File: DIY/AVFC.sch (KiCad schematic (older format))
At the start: 11 parts, among them J1 Conn_01x07, J2 Conn_01x07, J3 DB15_Female, J4 DB25_Male, U1 74AHCT125N, U2 74AHCT125N, U3 74AHCT125N, U4 74AHCT125N

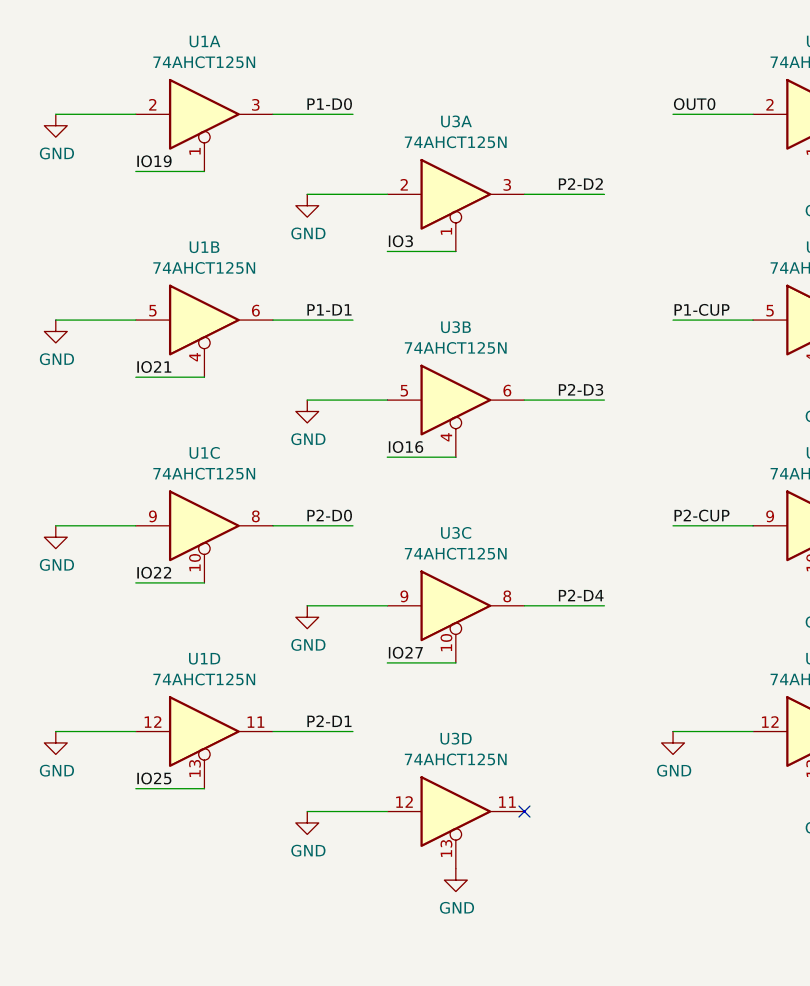
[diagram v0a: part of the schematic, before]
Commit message: Add pullup to OD outputs on ESP side
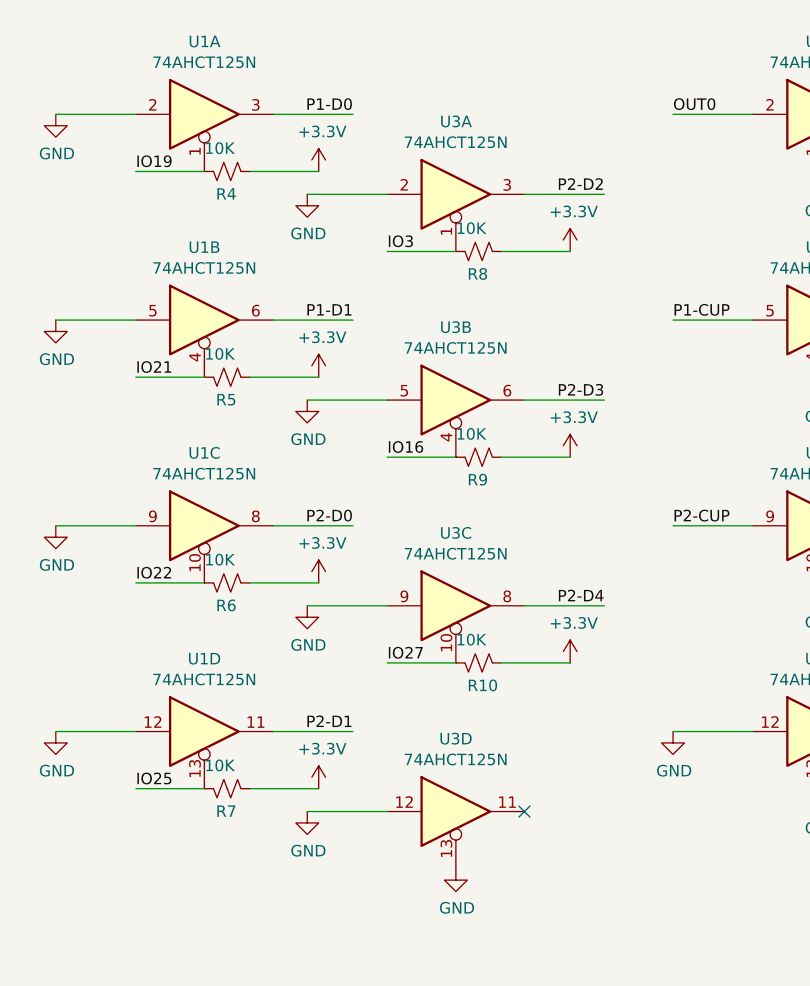
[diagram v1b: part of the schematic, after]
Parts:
- added R10, R4, R5, R6, R7, R8, R9: 10K, symbol Device:R_Small_US
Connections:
- net +3V3: now also R10.1, R4.1, R5.1, R6.1, R7.1, R8.1, R9.1
- net IO16: now also R9.2
- net IO19: now also R4.2
- net IO21: now also R5.2
- net IO22: now also R6.2
- net IO25: now also R7.2
- net IO27: now also R10.2
- net IO3: now also R8.2
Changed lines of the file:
@@
 Text Label 2200 4550 2    50   ~ 0
 P2-D2
+$Comp
+L power:+3.3V #PWR?
+U 1 1 6628EEDA
+P 3950 1600
+AR Path="/5F127084/6628EEDA" Ref="#PWR?"  Part="1"
+AR Path="/5F1E85DD/6628EEDA" Ref="#PWR?"  Part="1"
+AR Path="/65620D27/6628EEDA" Ref="#PWR?"  Part="1"
+F 0 "#PWR?" H 3950 1450 50  0001 C CNN
+F 1 "+3.3V" H 3965 1773 50  0000 C CNN
+F 2 "" H 3950 1600 50  0001 C CNN
+F 3 "" H 3950 1600 50  0001 C CNN
+	1    3950 1600
+	1    0    0    -1
+$EndComp
+$Comp
+L Device:R_Small_US R?
+U 1 1 6628EEE0
+P 3550 1600
+AR Path="/5F1E85DD/6628EEE0" Ref="R?"  Part="1"
+AR Path="/65620D27/6628EEE0" Ref="R4"  Part="1"
+F 0 "R4" V 3450 1550 50  0000 L CNN
+F 1 "10K" V 3650 1500 50  0000 L CNN
+F 2 "" H 3550 1600 50  0001 C CNN
+F 3 "~" H 3550 1600 50  0001 C CNN
+	1    3550 1600
+	0    1    -1   0
+$EndComp
+Wire Wire Line
+	3650 1600 3950 1600
+$Comp
+L power:+3.3V #PWR?
+U 1 1 662932E6
+P 3950 2500
+AR Path="/5F127084/662932E6" Ref="#PWR?"  Part="1"
+AR Path="/5F1E85DD/662932E6" Ref="#PWR?"  Part="1"
+AR Path="/65620D27/662932E6" Ref="#PWR?"  Part="1"
+F 0 "#PWR?" H 3950 2350 50  0001 C CNN
+F 1 "+3.3V" H 3965 2673 50  0000 C CNN
+F 2 "" H 3950 2500 50  0001 C CNN
+F 3 "" H 3950 2500 50  0001 C CNN
+	1    3950 2500
+	1    0    0    -1
+$EndComp
+$Comp
+L Device:R_Small_US R?
+U 1 1 662932EC
+P 3550 2500
+AR Path="/5F1E85DD/662932EC" Ref="R?"  Part="1"
+AR Path="/65620D27/662932EC" Ref="R5"  Part="1"
+F 0 "R5" V 3450 2450 50  0000 L CNN
+F 1 "10K" V 3650 2400 50  0000 L CNN
+F 2 "" H 3550 2500 50  0001 C CNN
+F 3 "~" H 3550 2500 50  0001 C CNN
+	1    3550 2500
+	0    1    -1   0
+$EndComp
+Wire Wire Line
+	3650 2500 3950 2500
+$Comp
+L power:+3.3V #PWR?
+U 1 1 66297501
+P 3950 3400
+AR Path="/5F127084/66297501" Ref="#PWR?"  Part="1"
+AR Path="/5F1E85DD/66297501" Ref="#PWR?"  Part="1"
+AR Path="/65620D27/66297501" Ref="#PWR?"  Part="1"
+F 0 "#PWR?" H 3950 3250 50  0001 C CNN
+F 1 "+3.3V" H 3965 3573 50  0000 C CNN
+F 2 "" H 3950 3400 50  0001 C CNN
+F 3 "" H 3950 3400 50  0001 C CNN
+	1    3950 3400
+	1    0    0    -1
+$EndComp
+$Comp
+L Device:R_Small_US R?
+U 1 1 66297507
+P 3550 3400
+AR Path="/5F1E85DD/66297507" Ref="R?"  Part="1"
+AR Path="/65620D27/66297507" Ref="R6"  Part="1"
+F 0 "R6" V 3450 3350 50  0000 L CNN
+F 1 "10K" V 3650 3300 50  0000 L CNN
+F 2 "" H 3550 3400 50  0001 C CNN
+F 3 "~" H 3550 3400 50  0001 C CNN
+	1    3550 3400
+	0    1    -1   0
+$EndComp
+Wire Wire Line
+	3650 3400 3950 3400
+$Comp
+L power:+3.3V #PWR?
+U 1 1 6629B5CB
+P 3950 4300
+AR Path="/5F127084/6629B5CB" Ref="#PWR?"  Part="1"
+AR Path="/5F1E85DD/6629B5CB" Ref="#PWR?"  Part="1"
+AR Path="/65620D27/6629B5CB" Ref="#PWR?"  Part="1"
+F 0 "#PWR?" H 3950 4150 50  0001 C CNN
+F 1 "+3.3V" H 3965 4473 50  0000 C CNN
+F 2 "" H 3950 4300 50  0001 C CNN
+F 3 "" H 3950 4300 50  0001 C CNN
+	1    3950 4300
+	1    0    0    -1
+$EndComp
+$Comp
+L Device:R_Small_US R?
+U 1 1 6629B5D1
+P 3550 4300
+AR Path="/5F1E85DD/6629B5D1" Ref="R?"  Part="1"
+AR Path="/65620D27/6629B5D1" Ref="R7"  Part="1"
+F 0 "R7" V 3450 4250 50  0000 L CNN
+F 1 "10K" V 3650 4200 50  0000 L CNN
+F 2 "" H 3550 4300 50  0001 C CNN
+F 3 "~" H 3550 4300 50  0001 C CNN
+	1    3550 4300
+	0    1    -1   0
+$EndComp
+Wire Wire Line
+	3650 4300 3950 4300
+$Comp
+L power:+3.3V #PWR?
+U 1 1 6629F3E8
+P 5050 1950
+AR Path="/5F127084/6629F3E8" Ref="#PWR?"  Part="1"
+AR Path="/5F1E85DD/6629F3E8" Ref="#PWR?"  Part="1"
+AR Path="/65620D27/6629F3E8" Ref="#PWR?"  Part="1"
+F 0 "#PWR?" H 5050 1800 50  0001 C CNN
+F 1 "+3.3V" H 5065 2123 50  0000 C CNN
+F 2 "" H 5050 1950 50  0001 C CNN
+F 3 "" H 5050 1950 50  0001 C CNN
+	1    5050 1950
+	1    0    0    -1
+$EndComp
+$Comp
+L Device:R_Small_US R?
+U 1 1 6629F3EE
+P 4650 1950
+AR Path="/5F1E85DD/6629F3EE" Ref="R?"  Part="1"
+AR Path="/65620D27/6629F3EE" Ref="R8"  Part="1"
+F 0 "R8" V 4550 1900 50  0000 L CNN
+F 1 "10K" V 4750 1850 50  0000 L CNN
+F 2 "" H 4650 1950 50  0001 C CNN
+F 3 "~" H 4650 1950 50  0001 C CNN
+	1    4650 1950
+	0    1    -1   0
+$EndComp
+Wire Wire Line
+	4750 1950 5050 1950
+$Comp
+L power:+3.3V #PWR?
+U 1 1 662A368F
+P 5050 2850
+AR Path="/5F127084/662A368F" Ref="#PWR?"  Part="1"
+AR Path="/5F1E85DD/662A368F" Ref="#PWR?"  Part="1"
+AR Path="/65620D27/662A368F" Ref="#PWR?"  Part="1"
+F 0 "#PWR?" H 5050 2700 50  0001 C CNN
+F 1 "+3.3V" H 5065 3023 50  0000 C CNN
+F 2 "" H 5050 2850 50  0001 C CNN
+F 3 "" H 5050 2850 50  0001 C CNN
+	1    5050 2850
+	1    0    0    -1
+$EndComp
+$Comp
+L Device:R_Small_US R?
+U 1 1 662A3695
+P 4650 2850
+AR Path="/5F1E85DD/662A3695" Ref="R?"  Part="1"
+AR Path="/65620D27/662A3695" Ref="R9"  Part="1"
+F 0 "R9" V 4550 2800 50  0000 L CNN
+F 1 "10K" V 4750 2750 50  0000 L CNN
+F 2 "" H 4650 2850 50  0001 C CNN
+F 3 "~" H 4650 2850 50  0001 C CNN
+	1    4650 2850
+	0    1    -1   0
+$EndComp
+Wire Wire Line
+	4750 2850 5050 2850
+$Comp
+L power:+3.3V #PWR?
+U 1 1 662A7B16
+P 5050 3750
+AR Path="/5F127084/662A7B16" Ref="#PWR?"  Part="1"
+AR Path="/5F1E85DD/662A7B16" Ref="#PWR?"  Part="1"
+AR Path="/65620D27/662A7B16" Ref="#PWR?"  Part="1"
+F 0 "#PWR?" H 5050 3600 50  0001 C CNN
+F 1 "+3.3V" H 5065 3923 50  0000 C CNN
+F 2 "" H 5050 3750 50  0001 C CNN
+F 3 "" H 5050 3750 50  0001 C CNN
+	1    5050 3750
+	1    0    0    -1
+$EndComp
+$Comp
+L Device:R_Small_US R?
+U 1 1 662A7B1C
+P 4650 3750
+AR Path="/5F1E85DD/662A7B1C" Ref="R?"  Part="1"
+AR Path="/65620D27/662A7B1C" Ref="R10"  Part="1"
+F 0 "R10" V 4550 3700 50  0000 L CNN
+F 1 "10K" V 4750 3650 50  0000 L CNN
+F 2 "" H 4650 3750 50  0001 C CNN
+F 3 "~" H 4650 3750 50  0001 C CNN
+	1    4650 3750
+	0    1    -1   0
+$EndComp
+Wire Wire Line
+	4750 3750 5050 3750
 $EndSCHEMATC
